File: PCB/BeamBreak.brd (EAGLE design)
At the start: 30.5 x 12.1 mm, 8 parts, among them J1 AUDIO-CONNECTOR-6P-SMD-344003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, Q1 MOSFET-N-0440200P1

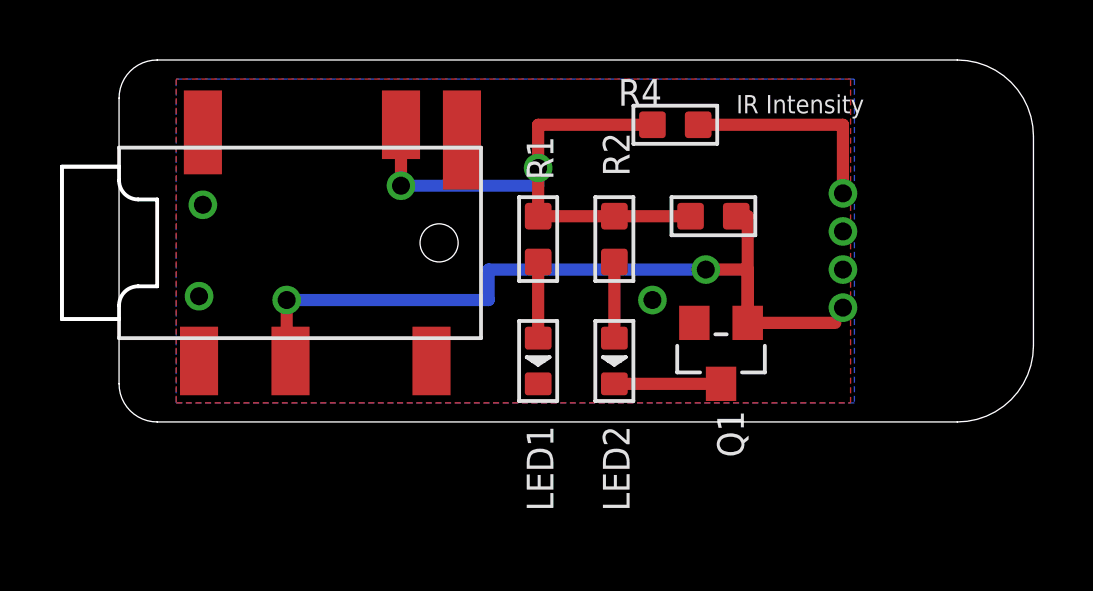
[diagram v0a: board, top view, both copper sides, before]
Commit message: Changed connections for wires to a header so that solder mask will be properly applied.
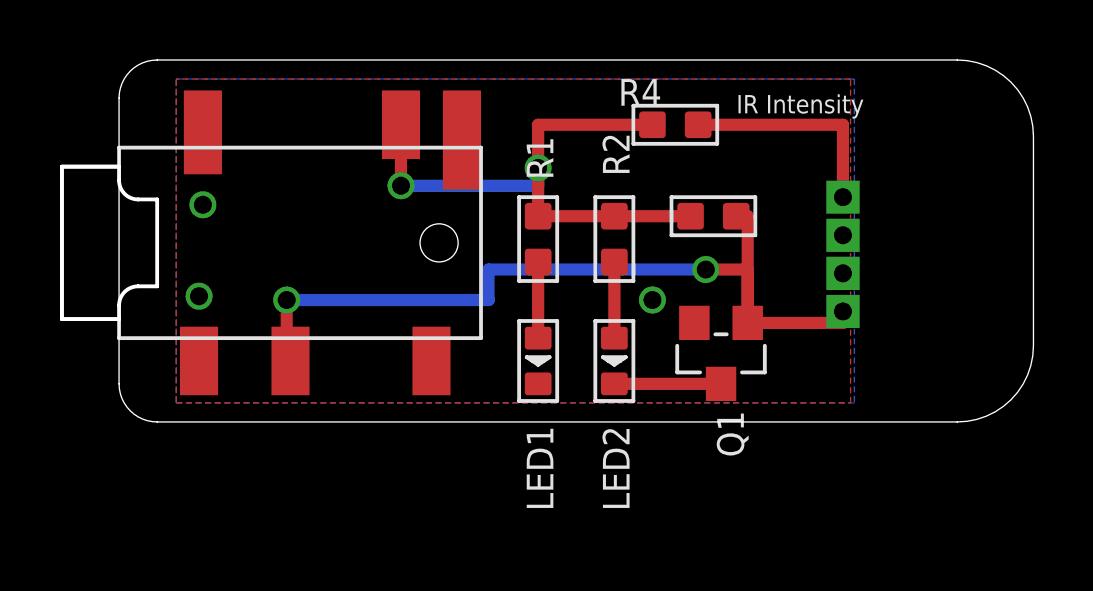
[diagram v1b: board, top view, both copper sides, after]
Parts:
- added U$1: HO4, BeamBreak:H04
- J1: device OPL:6P-SMD-3.5 -> BeamBreak:6P-SMD-3.5
- LED1, LED2: device OPL:LED0603 -> BeamBreak:LED0603
- Q1: device OPL:SOT23 -> BeamBreak:SOT23
- R1, R2, R3: device OPL:R0603 -> BeamBreak:R0603
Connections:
- net GND: now also U$1.2, U$1.3
- net IRLED: now also U$1.1
- net SIG: now also U$1.4
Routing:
- net SIG: track 27.2 -> 27.8 mm, vias 3 -> 2
- net IRLED: track 7.11 -> 7.24 mm, vias 1 -> 0
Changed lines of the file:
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@@
 </class>
 </classes>
-<designrules name="LaenPCBOrder">
+<designrules name="Seeed_DRU">
 <description language="de">&lt;b&gt;EAGLE Design Rules&lt;/b&gt;
 &lt;p&gt;
@@
 Einstellungen hier und speichern die Design Rules unter
 einem neuen Namen ab.</description>
-<description language="en">&lt;b&gt;Laen's PCB Order Design Rules&lt;/b&gt;
+<description language="en">&lt;b&gt;EAGLE Design Rules&lt;/b&gt;
 &lt;p&gt;
-Please make sure your boards conform to these design rules.</description>
+The default Design Rules have been set to cover
+a wide range of applications. Your particular design
+may have different requirements, so please make the
+necessary adjustments and save your customized
+design rules under a new name.</description>
+<description language="zh">&lt;b&gt;Seeed Studio EAGLE Design Rules&lt;/b&gt;
+</description>
 <param name="layerSetup" value="(1*16)"/>
-<param name="mtCopper" value="0.0356mm 0.0356mm 0.0356mm 0.0356mm 0.0356mm 0.0356mm 0.0356mm 0.0356mm 0.0356mm 0.0356mm 0.0356mm 0.0356mm 0.0356mm 0.0356mm 0.0356mm 0.0356mm"/>
-<param name="mtIsolate" value="1.5011mm 0.1499mm 0.2007mm 0.1499mm 0.2007mm 0.1499mm 0.2007mm 0.1499mm 0.2007mm 0.1499mm 0.2007mm 0.1499mm 0.2007mm 0.1499mm 0.2007mm"/>
+<param name="mtCopper" value="0.035mm 0.0175mm 0.035mm 0.035mm 0.035mm 0.035mm 0.035mm 0.035mm 0.035mm 0.035mm 0.035mm 0.035mm 0.035mm 0.035mm 0.0175mm 0.035mm"/>
+<param name="mtIsolate" value="1.5mm 1.1mm 0.2mm 0.15mm 0.2mm 0.15mm 0.2mm 0.15mm 0.2mm 0.15mm 0.2mm 0.15mm 0.2mm 0.15mm 0.2mm"/>
 <param name="mdWireWire" value="6mil"/>
 <param name="mdWirePad" value="6mil"/>
@@
 <param name="mdPadVia" value="6mil"/>
 <param name="mdViaVia" value="6mil"/>
-<param name="mdSmdPad" value="6mil"/>
-<param name="mdSmdVia" value="6mil"/>
-<param name="mdSmdSmd" value="6mil"/>
+<param name="mdSmdPad" value="0mil"/>
+<param name="mdSmdVia" value="0mil"/>
+<param name="mdSmdSmd" value="0mil"/>
 <param name="mdViaViaSameLayer" value="8mil"/>
 <param name="mnLayersViaInSmd" value="2"/>
-<param name="mdCopperDimension" value="15mil"/>
-<param name="mdDrill" value="6mil"/>
+<param name="mdCopperDimension" value="10mil"/>
+<param name="mdDrill" value="10mil"/>
 <param name="mdSmdStop" value="0mil"/>
 <param name="msWidth" value="6mil"/>
-<param name="msDrill" value="13mil"/>
-<param name="msMicroVia" value="13mil"/>
+<param name="msDrill" value="12mil"/>
+<param name="msMicroVia" value="12mil"/>
 <param name="msBlindViaRatio" value="0.5"/>
 <param name="rvPadTop" value="0.25"/>
@@
 <param name="rvMicroViaOuter" value="0.25"/>
 <param name="rvMicroViaInner" value="0.25"/>
-<param name="rlMinPadTop" value="7mil"/>
+<param name="rlMinPadTop" value="10mil"/>
 <param name="rlMaxPadTop" value="20mil"/>
-<param name="rlMinPadInner" value="7mil"/>
+<param name="rlMinPadInner" value="10mil"/>
 <param name="rlMaxPadInner" value="20mil"/>
-<param name="rlMinPadBottom" value="7mil"/>
+<param name="rlMinPadBottom" value="10mil"/>
 <param name="rlMaxPadBottom" value="20mil"/>
-<param name="rlMinViaOuter" value="7mil"/>
+<param name="rlMinViaOuter" value="6mil"/>
 <param name="rlMaxViaOuter" value="20mil"/>
-<param name="rlMinViaInner" value="7mil"/>
+<param name="rlMinViaInner" value="6mil"/>
 <param name="rlMaxViaInner" value="20mil"/>
 <param name="rlMinMicroViaOuter" value="4mil"/>
@@
 <param name="psTop" value="-1"/>
 <param name="psBottom" value="-1"/>
-<param name="psFirst" value="-1"/>
+<param name="psFirst" value="0"/>
 <param name="psElongationLong" value="100"/>
 <param name="psElongationOffset" value="100"/>
 <param name="mvStopFrame" value="1"/>
 <param name="mvCreamFrame" value="0"/>
-<param name="mlMinStopFrame" value="4mil"/>
-<param name="mlMaxStopFrame" value="4mil"/>
+<param name="mlMinStopFrame" value="2mil"/>
+<param name="mlMaxStopFrame" value="2mil"/>
 <param name="mlMinCreamFrame" value="0mil"/>
 <param name="mlMaxCreamFrame" value="0mil"/>
-<param name="mlViaStopLimit" value="0mil"/>
+<param name="mlViaStopLimit" value="100mil"/>
 <param name="srRoundness" value="0"/>
 <param name="srMinRoundness" value="0mil"/>
@@
 <param name="checkAngle" value="0"/>
 <param name="checkFont" value="1"/>
-<param name="checkRestrict" value="1"/>
+<param name="checkRestrict" value="0"/>
 <param name="useDiameter" value="13"/>
 <param name="maxErrors" value="50"/>
@@
 </autorouter>
 <elements>
-<element name="R3" library="OPL" package="R0603" value="25K" x="19.812" y="6.858" smashed="yes">
+<element name="R3" library="BeamBreak" package="R0603" value="25K" x="19.812" y="6.858" smashed="yes">
 <attribute name="VALUE" x="19.177" y="7.874" size="0.6096" layer="27"/>
 </element>
-<element name="R2" library="OPL" package="R0603" value="2K" x="16.51" y="6.096" smashed="yes" rot="R270">
+<element name="R2" library="BeamBreak" package="R0603" value="2K" x="16.51" y="6.096" smashed="yes" rot="R270">
 <attribute name="NAME" x="16.129" y="9.652" size="0.889" layer="25" ratio="11" rot="R270"/>
 <attribute name="VALUE" x="16.3195" y="6.731" size="0.508" layer="27" ratio="10" rot="R270"/>
 </element>
-<element name="R1" library="OPL" package="R0603" value="2K" x="13.97" y="6.096" smashed="yes" rot="R270">
+<element name="R1" library="BeamBreak" package="R0603" value="2K" x="13.97" y="6.096" smashed="yes" rot="R270">
 <attribute name="NAME" x="13.589" y="9.525" size="0.889" layer="25" ratio="11" rot="R270"/>
 <attribute name="VALUE" x="13.7795" y="6.731" size="0.508" layer="27" ratio="10" rot="R270"/>
 </element>
-<element name="J1" library="OPL" package="6P-SMD-3.5" value="AUDIO-CONNECTOR-6P-SMD-3440030P1" x="5.08" y="5.969" smashed="yes" rot="R180"/>
-<element name="LED1" library="OPL" package="LED0603" value="BLUE" x="13.97" y="2.032" smashed="yes" rot="R270">
+<element name="J1" library="BeamBreak" package="6P-SMD-3.5" value="AUDIO-CONNECTOR-6P-SMD-3440030P1" x="5.08" y="5.969" smashed="yes" rot="R180"/>
+<element name="LED1" library="BeamBreak" package="LED0603" value="BLUE" x="13.97" y="2.032" smashed="yes" rot="R270">
 <attribute name="NAME" x="13.589" y="-0.127" size="0.889" layer="25" ratio="11" rot="R270"/>
 <attribute name="VALUE" x="13.6525" y="3.175" size="0.635" layer="27" ratio="10" rot="R270"/>
 </element>
-<element name="LED2" library="OPL" package="LED0603" value="GREEN" x="16.51" y="2.032" smashed="yes" rot="R270">
+<element name="LED2" library="BeamBreak" package="LED0603" value="GREEN" x="16.51" y="2.032" smashed="yes" rot="R270">
 <attribute name="NAME" x="16.129" y="-0.127" size="0.889" layer="25" ratio="11" rot="R270"/>
 <attribute name="VALUE" x="16.1925" y="3.175" size="0.635" layer="27" ratio="10" rot="R270"/>
 </element>
-<element name="Q1" library="OPL" package="SOT23" value="MOSFET-N-0440200P1" x="20.066" y="2.286" smashed="yes" rot="R180">
+<element name="Q1" library="BeamBreak" package="SOT23" value="MOSFET-N-0440200P1" x="20.066" y="2.286" smashed="yes" rot="R180">
 <attribute name="NAME" x="19.939" y="0.381" size="0.889" layer="25" ratio="11" rot="R270"/>
 <attribute name="VALUE" x="21.336" y="4.064" size="0.635" layer="27" ratio="10" rot="R270"/>
 </element>
 <element name="R4" library="OPL" package="R0603" value="2K" x="18.542" y="9.906"/>
+<element name="U$1" library="BeamBreak" package="H04" value="HO4" x="24.13" y="5.588"/>
 </elements>
 <signals>
@@
 <via x="2.667" y="4.191" extent="1-16" drill="0.6" shape="square"/>
 <via x="17.78" y="4.064" extent="1-16" drill="0.6" shape="square"/>
-<via x="24.13" y="5.08" extent="1-16" drill="0.6" shape="square"/>
-<via x="24.13" y="6.35" extent="1-16" drill="0.6" shape="square"/>
+<contactref element="U$1" pad="2"/>
+<contactref element="U$1" pad="3"/>
 </signal>
 <signal name="VCC">
@@
 <wire x1="19.558" y1="5.08" x2="20.955" y2="5.08" width="0.4064" layer="1"/>
 <wire x1="20.955" y1="5.08" x2="20.955" y2="3.302" width="0.4064" layer="1"/>
-<wire x1="20.955" y1="3.302" x2="23.876" y2="3.302" width="0.4064" layer="1"/>
-<via x="24.13" y="3.81" extent="1-16" drill="0.6" shape="square"/>
-<wire x1="23.876" y1="3.302" x2="24.13" y2="3.81" width="0" layer="19" extent="1-1"/>
+<wire x1="20.955" y1="3.302" x2="24.13" y2="3.302" width="0.4064" layer="1"/>
+<contactref element="U$1" pad="4"/>
+<wire x1="24.13" y1="3.302" x2="24.13" y2="3.683" width="0.4064" layer="1"/>
 </signal>
 <signal name="N$1">
@@
 <signal name="IRLED">
 <contactref element="R4" pad="2"/>
-<via x="24.13" y="7.62" extent="1-16" drill="0.6" shape="square"/>
 <wire x1="19.304" y1="9.906" x2="24.13" y2="9.906" width="0.4064" layer="1"/>
-<wire x1="24.13" y1="9.906" x2="24.13" y2="7.62" width="0.4064" layer="1"/>
+<wire x1="24.13" y1="9.906" x2="24.13" y2="7.493" width="0.4064" layer="1"/>
+<contactref element="U$1" pad="1"/>
 </signal>
 <signal name="N$3">
